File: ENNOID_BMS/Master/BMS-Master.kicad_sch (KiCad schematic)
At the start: 35 parts, among them J1 Contactor+, J10 Charge, J11 CAN, J16 ISOSPI_TEMP, J18 OLED, J19 ISOSPI_CELL, J2 Cooling, J20 USB_C_Receptacle_USB2.0_16P, J21 INV_Power, J3 + 12V -, J4 Contactor-, J5 BAT_Power, J6 Power Button, J7 E-Stop, J8 Discharge, J9 Discharge, K1 SHV12-1A85-78L3K, Q1 BSS138

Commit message: Slave with SMD and no other fuses
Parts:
- removed BZ1: AI-1027-TWT-5V, ENNOID:BUZZER, symbol BMS-Master-rescue:Buzzer-Device-BMS-Master-rescue
- removed J18: OLED, Connector_Molex:Molex_KK-254_AE-6410-05A_1x05_P2.54mm_Vertical, symbol BMS-Master-rescue:Conn_01x05-Connector_Generic-BMS-Master-rescue
- removed J2: Cooling, ENNOID:Pin_1x02-XL, symbol BMS-Master-rescue:Conn_01x02-Connector_Generic-BMS-Master-rescue
- removed J20: USB_C_Receptacle_USB2.0_16P, ENNOID:SAMESKY_UJ20-C-H-G-SMT-1-P16-TR, symbol Connector:USB_C_Receptacle_USB2.0_16P
- removed J7: E-Stop, ENNOID:Pin_1x02-XL, symbol BMS-Master-rescue:Conn_01x02-Connector_Generic-BMS-Master-rescue
- removed J8: Discharge, ENNOID:Pin_1x02-XL, symbol BMS-Master-rescue:Conn_01x02-Connector_Generic-BMS-Master-rescue
- removed K1: SHV12-1A85-78L3K, ENNOID:SHV12-1AB5-7BL3K, symbol ENNOID:SHV12-1A85-78L3K
- removed Q1: BSS138, Package_TO_SOT_SMD:SOT-23, symbol Transistor_FET:BSS138
- removed R34, R44: 270, ENNOID:SM_3, symbol BMS-Master-rescue:R-Device-BMS-Master-rescue
- removed R4: 1.5k, Resistor_SMD:R_0603_1608Metric, symbol BMS-Master-rescue:R-Device-BMS-Master-rescue
- removed R42, R46, R50: 4.75k, Resistor_SMD:R_0603_1608Metric, symbol BMS-Master-rescue:R-Device-BMS-Master-rescue
- added J17: UJ20-C-H-G-SMT-1-P16-TR, Kicad_Libraries:SAMESKY_UJ20-C-H-G-SMT-1-P16-TR, symbol UJ20-C-H-G-SMT-1-P16-TR:UJ20-C-H-G-SMT-1-P16-TR
- J1: renamed from J5; footprint Connector_Phoenix_GMSTB:PhoenixContact_GMSTBVA_2,5_2-G_1x02_P7.50mm_Vertical -> Kicad_Libraries:Phoenix_1x2_1729128; MPN 30.102 -> 1729128
- J10: value Charge -> LVE_Shutdown; footprint ENNOID:Pin_1x02-XL -> Connector_JST:JST_XH_B2B-XH-A_1x02_P2.50mm_Vertical; MPN 70543-0001 -> B2B-XH-A
- J11: footprint Connector_Molex:Molex_KK-254_AE-6410-05A_1x05_P2.54mm_Vertical -> Connector_JST:JST_XH_B5B-XH-A_1x05_P2.50mm_Vertical; MPN 70543-0004 -> B5B-XH-A
- J4: renamed from J3; footprint ENNOID:Pin_1x02-XL -> Connector_JST:JST_XH_B2B-XH-A_1x02_P2.50mm_Vertical
- J5: renamed from J6; footprint Connector_Molex:Molex_KK-254_AE-6410-05A_1x05_P2.54mm_Vertical -> Connector_JST:JST_XH_B5B-XH-A_1x05_P2.50mm_Vertical; MPN 282834-5 -> B5B-XH-A
- J6: renamed from J21; footprint Connector_Phoenix_GMSTB:PhoenixContact_GMSTBVA_2,5_2-G_1x02_P7.50mm_Vertical -> Kicad_Libraries:Phoenix_1x2_1729128; MPN 30.102 -> 1729128
- J7: renamed from J19; footprint ENNOID:Pin_1x02-XL -> Connector_JST:JST_XH_B2B-XH-A_1x02_P2.50mm_Vertical; MPN 70543-0001 -> B2B-XH-A
- J8: renamed from J16; footprint ENNOID:Pin_1x02-XL -> Connector_JST:JST_XH_B2B-XH-A_1x02_P2.50mm_Vertical; MPN 70543-0001 -> B2B-XH-A
- J9: value Discharge -> Charger_Shutdown; footprint ENNOID:Pin_1x02-XL -> Connector_JST:JST_XH_B2B-XH-A_1x02_P2.50mm_Vertical; MPN 70543-0001 -> B2B-XH-A
- R4: renamed from R52; MPN (none) -> RC0603JR-075K1L
- R5: renamed from R53; MPN (none) -> RC0603JR-075K1L
- renumbered D21 to D1, D20 to D2, D1 to D3, D2 to D4, J1 to J2, J4 to J3, R2 to R1, R1 to R2
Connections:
- net +12V: no longer J10.1 (Pin_1), J9.1 (Pin_1)
- net GND: now also J17.A1_B12 (GND), J17.B1_A12 (GND), J17.SH1 (SHIELD), J17.SH2 (SHIELD), J17.SH3 (SHIELD), J17.SH4 (SHIELD)
- net USB/D+: now also J17.A6 (DP1), J17.B6 (DP2)
- net USB/D-: now also J17.A7 (DN1), J17.B7 (DN2)
- net USB/Vusb: now also J17.A4_B9 (VBUS), J17.B4_A9 (VBUS)
- net BMS_OK/Charge_enable_S: now reaches J9.2 (Pin_2)
- net at R5.1: now also J17.A5 (CC1)
- net at R4.1: now also J17.B5 (CC2)
- net switches/Charge renamed BMS_OK/Discharge_enable_S
- new net BMS_OK/Charger_Safety_S: J9.1 (Pin_1)
- new net BMS_OK/Multipurpose_enable_S: J10.1 (Pin_1)
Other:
- removed sheet switches
- added sheet BMS_OK (BMS_OK.kicad_sch)
- sheet MCU ports: added Charge_enable, Charger_Safey, Discharge_enable, Multipurpose_enable; removed BUZZER, ChargeEnable, CoolingEnable, DischargeNegEnable, DischargePosEnable, NTC_Switch, OLED_RST, OLED_SCL, OLED_SDA, PreChargeEnable, Safety
- note added: "flow could be teensy requests charge over CAN to the BMS, BMS decides on charge enable and safety conditions, shtudown circuit closes."
- note removed: "This charge pin can be used as the enable pin of the charger. flow could be teensy requests charge over CAN to the BMS, BMS decides on charge enable and safety conditions, shtudown circuit closes, and charger enable switch goes high/low"
- note removed: "This is for debugging screen probably not necessary"
- note removed: "this relay can be cut"
- moved on the sheet: R4, R5

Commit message: master and slave updated
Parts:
- J4: MPN 70543-0001 -> B2B-XH-A
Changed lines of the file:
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@@
 			)
 		)
-		(property "MPN" "70543-0001 "
+		(property "MPN" "B2B-XH-A"
 			(at 87.63 91.44 0)
 			(effects

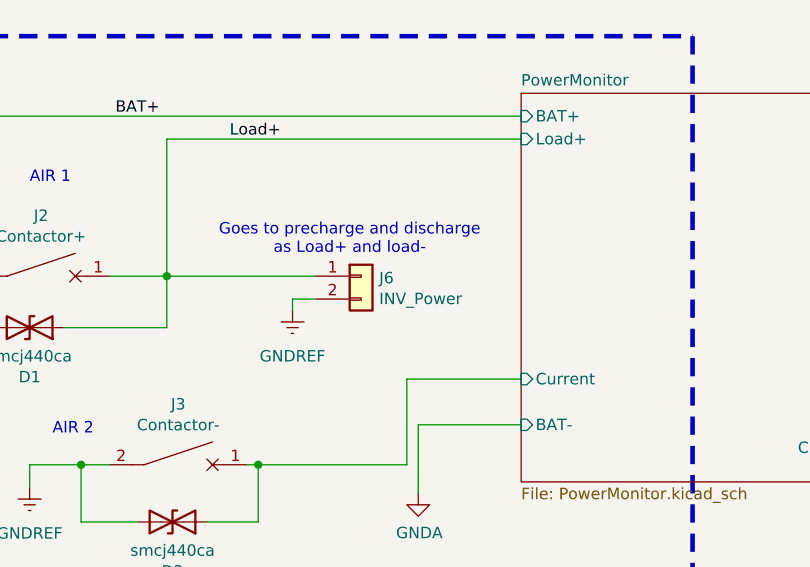
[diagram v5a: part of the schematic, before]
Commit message: new cells and updated slave
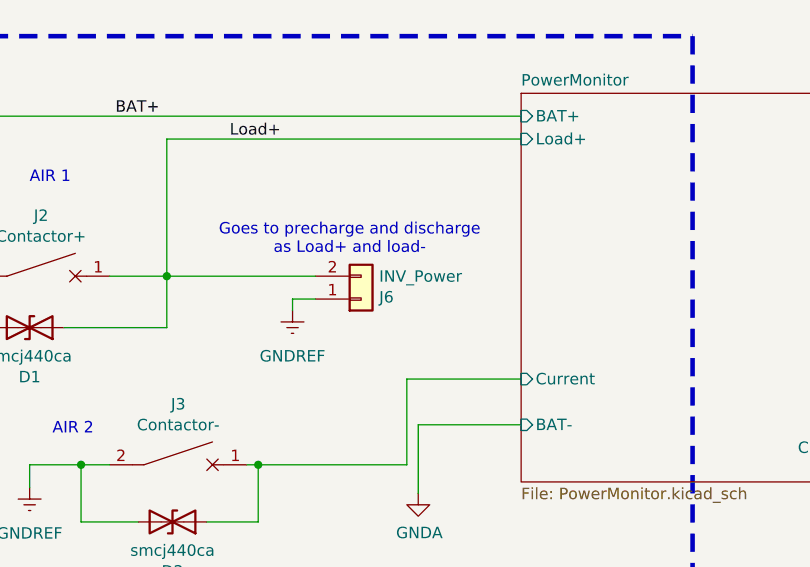
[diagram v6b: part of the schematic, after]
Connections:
- net GNDREF: now also J6.1 (Pin_1); no longer J6.2 (Pin_2)
- net Load+: now also J6.2 (Pin_2); no longer J6.1 (Pin_1)
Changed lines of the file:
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@@
 	(wire
 		(pts
-			(xy 85.09 43.18) (xy 87.63 43.18)
-		)
-		(stroke
-			(width 0)
-			(type default)
-		)
-	)
-	(wire
-		(pts
 			(xy 55.88 61.595) (xy 55.88 64.135)
 		)
@@
 	(wire
 		(pts
+			(xy 71.12 40.64) (xy 87.63 40.64)
+		)
+		(stroke
+			(width 0)
+			(type default)
+		)
+	)
+	(wire
+		(pts
 			(xy 29.845 44.45) (xy 29.845 43.18)
 		)
@@
 	(wire
 		(pts
-			(xy 71.12 40.64) (xy 87.63 40.64)
-		)
-		(stroke
-			(width 0)
-			(type default)
-		)
-	)
-	(wire
-		(pts
 			(xy 308.61 180.34) (xy 304.8 180.34)
 		)
@@
 		)
 	)
+	(wire
+		(pts
+			(xy 85.09 43.18) (xy 87.63 43.18)
+		)
+		(stroke
+			(width 0)
+			(type default)
+		)
+	)
 	(label "BAT+"
 		(at 65.405 22.86 0)
@@
 	(symbol
 		(lib_id "BMS-Master-rescue:Conn_01x02-Connector_Generic-BMS-Master-rescue")
-		(at 92.71 40.64 0)
+		(at 92.71 43.18 0)
+		(mirror x)
 		(unit 1)
 		(exclude_from_sim no)
@@
 		(dnp no)
 		(property "Reference" "J6"
-			(at 94.7166 40.8432 0)
+			(at 94.7166 42.9768 0)
 			(effects
 				(font
@@
 		)
 		(property "Value" "INV_Power"
-			(at 94.7166 43.1546 0)
+			(at 94.7166 40.6654 0)
 			(effects
 				(font
@@
 		)
 		(property "Footprint" "Kicad_Libraries:Phoenix_1x2_1729128"
-			(at 92.71 40.64 0)
+			(at 92.71 43.18 0)
 			(effects
 				(font
@@
 		)
 		(property "Datasheet" "https://www.phoenixcontact.com/en-us/products/printed-circuit-board-terminal-mkdsn-15-2-508-1729128?type=pdf"
-			(at 92.71 40.64 0)
+			(at 92.71 43.18 0)
 			(effects
 				(font
@@
 		)
 		(property "Description" ""
-			(at 92.71 40.64 0)
+			(at 92.71 43.18 0)
 			(effects
 				(font
@@
 		)
 		(property "MPN" "1729128"
-			(at 92.71 40.64 0)
+			(at 92.71 43.18 0)
 			(effects
 				(font

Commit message: added author
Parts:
- removed LOGO1: Logo_Open_Hardware_Small, ENNOID:ENNOID-LOGO, symbol Graphic:Logo_Open_Hardware_Small
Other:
- company: ENNOID -> UCD Formula Student
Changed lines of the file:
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@@
 		(title "BMS-Master")
 		(rev "V0.1")
-		(company "ENNOID")
+		(company "UCD Formula Student")
+		(comment 1 "Author: Keelan Reilly")
 	)
 	(text "Ground domains:\n	•	GND: Low-voltage logic ground (MCU, CAN, I²C)\n	•	GNDA: Accumulator negative (BAT−, TS−)\n	•	GNDREF: Vehicle-side HV negative (Load−, inverter DC-link reference)\nGNDA and GNDREF are connected only when the negative AIR is closed."
@@
 					(unit 1)
 				)
-			)
-		)
-	)
-	(symbol
-		(lib_id "Graphic:Logo_Open_Hardware_Small")
-		(at 318.77 260.35 0)
-		(unit 1)
-		(exclude_from_sim no)
-		(in_bom yes)
-		(on_board yes)
-		(dnp no)
-		(property "Reference" "LOGO1"
-			(at 318.77 253.365 0)
-			(effects
-				(font
-					(size 1.27 1.27)
-				)
-				(hide yes)
-			)
-		)
-		(property "Value" "Logo_Open_Hardware_Small"
-			(at 318.77 266.065 0)
-			(effects
-				(font
-					(size 1.27 1.27)
-				)
-				(hide yes)
-			)
-		)
-		(property "Footprint" "ENNOID:ENNOID-LOGO"
-			(at 318.77 260.35 0)
-			(effects
-				(font
-					(size 1.27 1.27)
-				)
-				(hide yes)
-			)
-		)
-		(property "Datasheet" "~"
-			(at 318.77 260.35 0)
-			(effects
-				(font
-					(size 1.27 1.27)
-				)
-				(hide yes)
-			)
-		)
-		(property "Description" ""
-			(at 318.77 260.35 0)
-			(effects
-				(font
-					(size 1.27 1.27)
-				)
-			)
-		)
-		(property "MPN" "N/A"
-			(at 318.77 260.35 0)
-			(effects
-				(font
-					(size 1.27 1.27)
-				)
-				(hide yes)
-			)
-		)
-		(instances
-			(project ""
-				(path "/b08f1666-8d98-49de-9988-f6179a2f79fe"
-					(reference "LOGO1")
-					(unit 1)
-				)
